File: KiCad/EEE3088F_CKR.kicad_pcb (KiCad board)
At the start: 2 copper layers, 129 parts, among them J1 Conn_01x02_Pin, J2 Conn_01x02_Pin, J4 Debugger, Q1 AO3401A, Q2 AO3401A, Q3 AO3401A, Q4 AO3401A, Q5 AO3401A, Q6 AO3401A, Q7 AO3401A, SW1 Reset switch, SW2 switch, SW3 switch, SW4 switch, U1 Battery Charger, U2 LMV321, U3 XC6206PxxxMR, U4 GXHTC3, U5 LTR-303ALS-01, U7 24LC256, U8 usb, U9 HT42B534-2, u6 batter hoder

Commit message: lots of PCB stuff
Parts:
- removed TP12: TempHum SDA, footprint:Testpoint_2.54mm
- removed TP13: TempHum SCL, footprint:Testpoint_2.54mm
- TP2: value batter charger -> battery charger
- TP4: value +batter out -> +battery out
- TP5: value revers polarety -> reverse polarity
- u6: value batter hoder -> battery holder
- moved J2 338.1 mm to (-121.5, 61.3), turned to -90 degrees
- moved u6 295.1 mm to (-75.0, 62.5), turned to 90 degrees
- moved R25 284.9 mm to (-115.0, 136.2), turned to 90 degrees
- moved C5 282.2 mm to (-118.0, 123.5), turned to 90 degrees
- moved C6 278.5 mm to (-116.0, 118.7), turned to -90 degrees
- moved U5 275.6 mm to (-113.5, 118.1), turned to -90 degrees
- moved TP8 271.7 mm to (-111.5, 134.5)
- moved TP11 268.8 mm to (-107.5, 121.5)
- moved R22 266.5 mm to (-115.0, 131.2), turned to 90 degrees
- moved U2 265.7 mm to (-67.0, 83.0), turned to 90 degrees
- moved Q5 263.4 mm to (-108.5, 131.2), turned to 90 degrees
- moved R26 262.9 mm to (-115.0, 126.2), turned to -90 degrees
- moved R24 262.6 mm to (-112.5, 131.2), turned to 90 degrees
- moved TP9 262.2 mm to (-107.5, 118.0)
- moved C3 261.9 mm to (-55.0, 97.0), turned to 90 degrees
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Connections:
- R21 pad 2: +3.3V -> +3V3
- R22 pad 2: +3.3V -> +3V3
- R23 pad 2: +3.3V -> +3V3
- R24 pad 2: +3.3V -> +3V3
- R26 pad 2: +3.3V -> +3V3
- R27 pad 2: +3.3V -> +3V3
- R28 pad 2: +3.3V -> +3V3
- R29 pad 2: +3.3V -> +3V3
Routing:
- net +3V3: track 0.00 -> 404.2 mm
- net /Microcontroller/SDA_1: track 0.00 -> 57.5 mm, vias 0 -> 1
- net /Microcontroller/NSRT: track 0.00 -> 56.0 mm
- net Net-(D1-A): track 0.00 -> 34.5 mm, vias 0 -> 2
- net Net-(U8-D+): track 0.00 -> 33.5 mm, vias 0 -> 4
- net /Microcontroller/Lght_P_2: track 0.00 -> 30.0 mm, vias 0 -> 2
- net +5V: track 0.00 -> 29.7 mm, vias 0 -> 2
- net Net-(Q1-S): track 0.00 -> 29.5 mm, vias 0 -> 4
- net Net-(U8-D-): track 0.00 -> 28.2 mm, vias 0 -> 1
- net Net-(J1-Pin_2): track 0.00 -> 27.7 mm
- net Net-(U1-BAT): track 0.00 -> 17.1 mm
- net /Power/3.3V UVLO/polarity protector: track 0.00 -> 17.0 mm
- net /Microcontroller/Potentiometer_signal: track 0.00 -> 16.1 mm
- net /Power/polarity protected battery voltage: track 0.00 -> 16.1 mm
- net /Microcontroller/Thermistor_signal: track 0.00 -> 15.7 mm
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- added copper zone on B.Cu, net GND
- added copper zone on F.Cu, net GND
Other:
- board outline added: 100 x 100 mm
- board text removed: "LDO"
- board text removed: "UVLO"
- board text removed: "revers polarety 2"

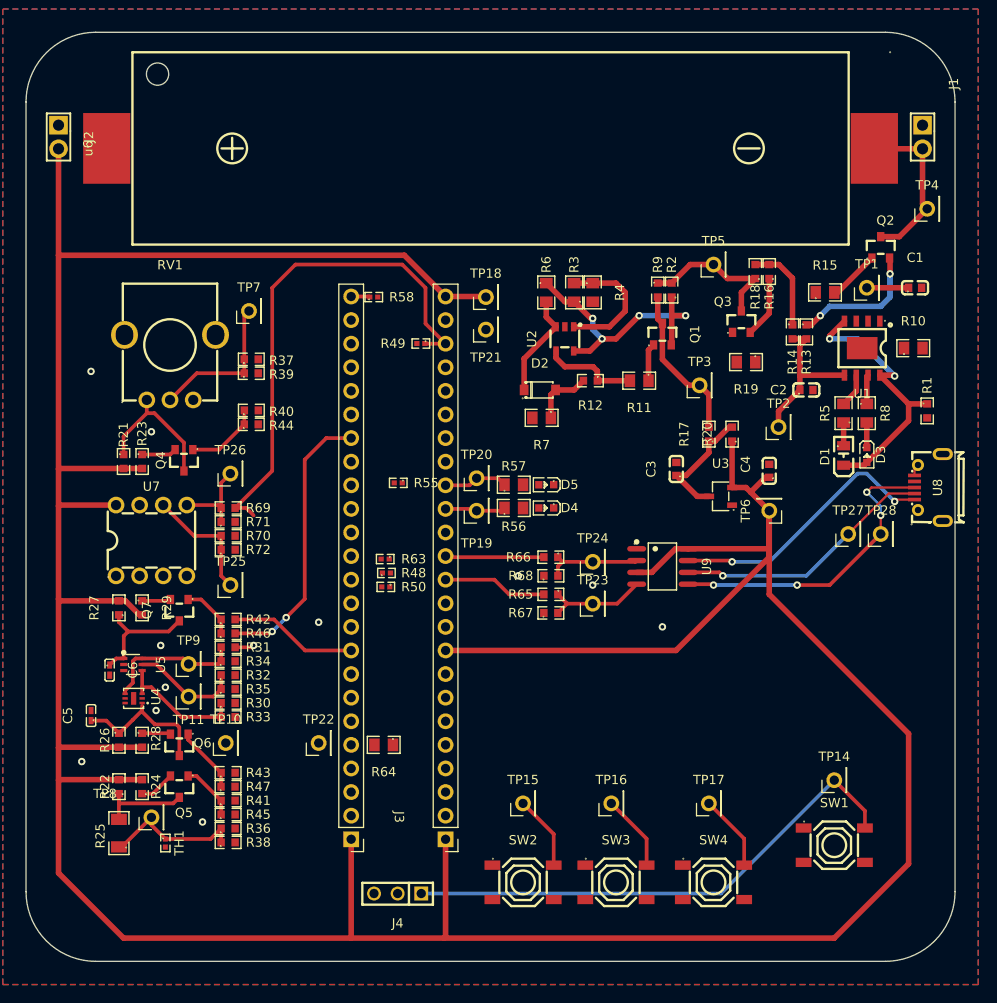
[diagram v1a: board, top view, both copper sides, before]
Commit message: the PCB suffered - wired up the micro controller
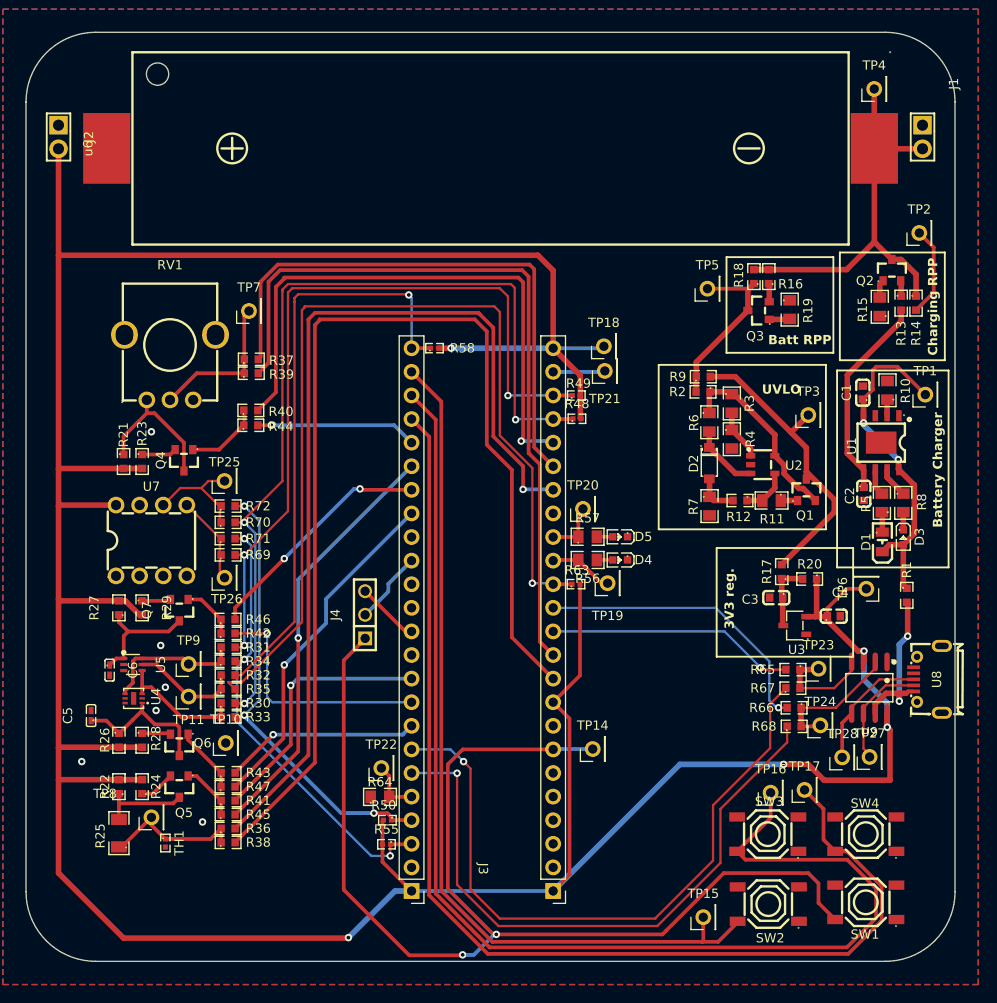
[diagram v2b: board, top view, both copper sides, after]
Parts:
- moved R55 38.9 mm to (-86.2, 137.4)
- moved R66 30.8 mm to (-42.3, 122.7)
- moved R68 30.8 mm to (-42.3, 124.7)
- moved J4 30.2 mm to (-88.5, 112.7), turned to 90 degrees
- moved TP24 30.2 mm to (-39.5, 124.6)
- moved R65 27.3 mm to (-42.5, 118.6)
- moved R67 27.3 mm to (-42.5, 120.6)
- moved SW2 26.5 mm to (-45.1, 143.8), turned to 180 degrees
- moved R48 26.4 mm to (-65.7, 91.6)
- moved TP14 26.2 mm to (-64.0, 127.2)
- moved U9 25.8 mm to (-34.2, 120.5), turned to 180 degrees
- moved TP2 25.8 mm to (-28.9, 71.6)
- moved TP23 25.3 mm to (-39.7, 118.5)
- moved U2 25.2 mm to (-45.7, 96.5), turned to 180 degrees
- moved R50 25.1 mm to (-86.1, 134.8)
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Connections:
- J3 pad 7: unconnected-(J3-_NSRT-Pad7) -> /Microcontroller/NSRT
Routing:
- net /Microcontroller/SW2: track 8.22 -> 133.4 mm
- net /Microcontroller/THM_2: track 0.00 -> 118.9 mm
- net /Microcontroller/SW3: track 8.22 -> 123.9 mm
- net /Microcontroller/INT_2: track 0.00 -> 102.0 mm, vias 0 -> 1
- net /Microcontroller/THM_1: track 0.00 -> 100.9 mm, vias 0 -> 1
- net /Microcontroller/SCL_1: track 0.00 -> 96.3 mm, vias 0 -> 3
- net /Microcontroller/SW1: track 8.02 -> 95.0 mm
- net /Microcontroller/POT_2: track 0.00 -> 80.9 mm
- net /Microcontroller/Tx_1: track 0.00 -> 72.0 mm, vias 0 -> 1
- net /Microcontroller/NSRT: track 56.0 -> 127.7 mm, vias 0 -> 2
- net /Microcontroller/Rx_1: track 0.00 -> 67.6 mm, vias 0 -> 1
- net /Microcontroller/POT_P_1: track 0.00 -> 62.1 mm, vias 0 -> 1
- net /Microcontroller/INT_1: track 2.02 -> 64.1 mm, vias 0 -> 1
- net /Microcontroller/POT_1: track 0.00 -> 60.9 mm
- net /Microcontroller/SCL_2: track 0.00 -> 48.9 mm, vias 0 -> 3
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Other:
- board text added: "3V3 reg."
- board text added: "Batt RPP"
- board text added: "Battery Charger"
- board text added: "Charging RPP"
- board text added: "UVLO"
